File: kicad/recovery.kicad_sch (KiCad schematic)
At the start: 88 parts, among them CN1 S08B-PASK-2(LF)(SN), J1 Bus_PCI_Express_x1, J2 wago 2060-452/998-404, J3 wago 2060-452/998-404, J4 Conn_01x04, J5 Conn_01x02_Pin, J6 USB_C_Receptacle_USB2.0_16P, Q1 SI7232DN-T1-GE3, Q2 AO3400A, Q3 AO3400A, U1 MCP6002T-I/SN, U12 S03B-PASK-2, U13 S03B-PASK-2, U2 RP2040, U4 W25Q128JVP, U5 TPS22976DPUR, U6 GAQY252G3S, U9 MCP25625T-E/ML, X1 RP2040 Crystal, Y2 X322516MLB4SI

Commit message: feat: overhauled recovery board: added servos, solenoids, PWM-level shifters and firing circuit to layout
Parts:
- removed C2, C3: 100pF, PCM_JLCPCB:C_0402, symbol PCM_JLCPCB-Capacitors:0402,100pF
- removed C31: 22nF, PCM_JLCPCB:C_0603, symbol PCM_JLCPCB-Capacitors:0603,22nF
- removed CN1: S08B-PASK-2(LF)(SN), easyeda2kicad:CONN-TH_S08B-PASK-2, symbol easyeda2kicad:S08B-PASK-2(LF)(SN)
- removed R1, R9: 100Ω, PCM_JLCPCB:R_0402, symbol PCM_JLCPCB-Resistors:0402,100Ω
- removed R203, R204: 27, Resistor_SMD:R_0402_1005Metric, symbol Device:R
- removed R29, R34: 5.1Ω, PCM_JLCPCB:R_0603, symbol PCM_JLCPCB-Resistors:0603,5.1Ω
- removed U12: S03B-PASK-2, easyeda2kicad:CONN-TH_S03B-PASK-2-LF-SN, symbol easyeda2kicad:S03B-PASK-2(LF)(SN)
- added C2, C4: 100pF, PCM_JLCPCB:C_0603, symbol PCM_JLCPCB-Capacitors:0603,100pF
- added C3, C5, C6, C7, C8: 100u, Capacitor_SMD:C_1210_3225Metric, symbol Device:C
- added R1, R36: 100Ω, PCM_JLCPCB:R_0603, symbol PCM_JLCPCB-Resistors:0603,100Ω
- added R35: 27Ω, PCM_JLCPCB:R_0603, symbol PCM_JLCPCB-Resistors:0603,27Ω
- added U10: S03B-PASK-2, easyeda2kicad:CONN-TH_S03B-PASK-2-LF-SN, symbol easyeda2kicad:S03B-PASK-2(LF)(SN)
- added U3, U7: MOF5WS-5.1Ω±5% T, easyeda2kicad:RES-TH_BD6.0-L17.5-P21.50-D0.7, symbol easyeda2kicad:MOF5WS-5.1Ω±5%T
- added U8: S05B-PASK-2(LF)(SN), easyeda2kicad:CONN-TH_S05B-PASK-2-LF-SN, symbol easyeda2kicad:S05B-PASK-2(LF)(SN)
- R11: now fitted
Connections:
- net +5V_Servo is gone; now on net +5V: C21.1, C28.1, R19.2, R24.2, U5.1 (VIN1), U5.2 (VIN1), U5.4 (VBIAS), U5.6 (VIN2), U5.7 (VIN2)
- net AIN_0IN is gone; now on net PT_IN1: U13.2
- net AIN_1IN is gone; now on net PT_IN2: U13.3
- net +24V: now also U10.3
- net +3.3V: no longer R10.1, R15.1, R16.2, R17.2, R18.1
- net +5V: now also C3.1, C5.1, C6.1, C7.1, C8.1
- net 5V_PWM1: now also U8.5
- net 5V_PWM2: now also U8.1
- net CANSTBY: now also U2.18 (GPIO15)
- net GND: now also C2.2, C3.2, C4.2, C5.2, C6.2, C7.2, C8.2, U10.1, U10.2, U8.3; no longer R11.2
- net OUTA: now also R36.2
- net OUTB: now also R1.2
- net PT_1: now also C4.1, R36.1
- net PT_2: now also C2.1, R1.1
- net SERVO_PWR1: now also U8.4
- net SERVO_PWR2: now also U8.2
- net SWCLK: now also J4.2 (Pin_2); no longer J4.1 (Pin_1)
- net SWD: now also J4.1 (Pin_1); no longer J4.2 (Pin_2)
- net USB_D+: now also R35.1
- net USB_D-: now also R11.1
- net USB_D2+: now also R35.2
- net USB_D2-: now also R11.2
- net at Q1.7, Q1.8, R32.2: now also U7.1
- net at Q1.5, Q1.6, R22.2: now also U3.1
- net MCU_SOLENOID: now reaches U2.3 (GPIO1)
- net MCU_SOLENOID: now also R10.1
- net at J2.1 (1_1), J2.2 (1_2): now also U7.2
- net at J3.1 (1_1), J3.2 (1_2): now also U3.2
- new net MCU_PWM1: R15.1, R16.2
- new net MCU_PWM2: R17.2, R18.1
- no-connect marks 35 -> 31
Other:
- moved on the sheet: C1, J4, U13

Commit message: Feat: Completed layout, modified divider network for 5V PT operation
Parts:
- removed C21, C28: 1uF, PCM_JLCPCB:C_0603, symbol PCM_JLCPCB-Capacitors:0603,1uF
- removed C29, C30: 100nF, PCM_JLCPCB:C_0402, symbol PCM_JLCPCB-Capacitors:0402,100nF
- removed C5, C6, C7, C8: 100u, Capacitor_SMD:C_1210_3225Metric, symbol Device:C
- removed R13, R14, R16, R17, R19, R24: 5.1kΩ, PCM_JLCPCB:R_0603, symbol PCM_JLCPCB-Resistors:0603,5.1kΩ
- removed R15, R18: 120Ω, PCM_JLCPCB:R_0603, symbol PCM_JLCPCB-Resistors:0603,120Ω
- removed R25: 10kΩ, PCM_JLCPCB:R_0402, symbol PCM_JLCPCB-Resistors:0402,10kΩ
- removed R27, R28: 10Ω, PCM_JLCPCB:R_0603, symbol PCM_JLCPCB-Resistors:0603,10Ω
- removed R5, R7: 100kΩ, PCM_JLCPCB:R_0402, symbol PCM_JLCPCB-Resistors:0402,100kΩ
- removed R6, R8: 33kΩ, PCM_JLCPCB:R_0402, symbol PCM_JLCPCB-Resistors:0402,33kΩ
- removed U10: S03B-PASK-2, easyeda2kicad:CONN-TH_S03B-PASK-2-LF-SN, symbol easyeda2kicad:S03B-PASK-2(LF)(SN)
- removed U5: TPS22976DPUR, easyeda2kicad:WSON-14_L3.0-W2.0-P0.40-BL-EP-1, symbol easyeda2kicad:TPS22976DPUR
- removed U8: S05B-PASK-2(LF)(SN), easyeda2kicad:CONN-TH_S05B-PASK-2-LF-SN, symbol easyeda2kicad:S05B-PASK-2(LF)(SN)
- added C12, C13, C9: 100u, Capacitor_SMD:C_1210_3225Metric, symbol Device:C
- added C5, C6, C7, C8: 1uF, PCM_JLCPCB:C_0402, symbol PCM_JLCPCB-Capacitors:0402,1uF
- added CN1: S06B-PASK-2(LF)(SN), easyeda2kicad:CONN-TH_6P-P2.00_S06B-PASK-2-LF-SN, symbol easyeda2kicad:S06B-PASK-2(LF)(SN)
- added R13, R14, R9: 10kΩ, PCM_JLCPCB:R_0402, symbol PCM_JLCPCB-Resistors:0402,10kΩ
- added R15, R16: 1k, Resistor_SMD:R_0402_1005Metric, symbol Device:R
- added R18, R6: 100kΩ, PCM_JLCPCB:R_0603, symbol PCM_JLCPCB-Resistors:0603,100kΩ
- added R5, R7: 51kΩ, PCM_JLCPCB:R_0603, symbol PCM_JLCPCB-Resistors:0603,51kΩ
- added U11, U5: TMI6240, easyeda2kicad:SOT-23-5_L2.9-W1.6-P0.95-LS2.8-BL, symbol easyeda2kicad:TMI6240
- added U8: S02B-PASK-2(LF)(SN), easyeda2kicad:CONN-TH_S02B-PASK-2-LF-SN, symbol easyeda2kicad:S02B-PASK-2(LF)(SN)
- C1, C3: LCSC (none) -> C23742
- C10, C11: LCSC (none) -> C1548
- C2, C4: LCSC PN (none) -> C14858
- C206, C207, C209, C211, C212, C213, C214, C215, C216, C40, C90, C92, C93: LCSC (none) -> C307331
- C208, C210: LCSC (none) -> C52923
- C94, C95: LCSC (none) -> C1555
- D1: LCSC (none) -> C2286
- D2: LCSC PN (none) -> C14996
- J2, J3: LCSC (none) -> C2765055
- J6: LCSC (none) -> C2765186
- Q1: LCSC (none) -> C144854
- Q2, Q3: LCSC PN (none) -> C20917
- R1, R36: LCSC PN (none) -> C22775
- R10: LCSC PN (none) -> C23025
- R11, R35: LCSC PN (none) -> C25190
- R12, R2, R30: LCSC (none) -> C11702
- R20, R300: LCSC (none) -> C25076
- R21, R31: LCSC (none) -> C25890
- R22, R32: LCSC (none) -> C25741
- R23, R33: LCSC (none) -> C25551
- R3, R4: LCSC (none) -> C25905
- R91: LCSC (none) -> C25744
- S2: LCSC (none) -> C318884
- U1: LCSC (none) -> C7377
- U13: LCSC (none) -> C265095
- U2: LCSC (none) -> C2040
- U3, U7: LCSC (none) -> C121946
- U4: LCSC (none) -> C190862
- U6: LCSC (none) -> C7435106
- U9: LCSC (none) -> C191253
- X1: LCSC (none) -> C20625731
- Y2: LCSC (none) -> C12668
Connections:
- net 3.3V_PWM1 is gone; now on net MCU_PWM1: Q2.2 (S)
- net +24V: now also D2.1, U8.2; no longer D2.2
- net +3.3V: now also R9.2
- net +5V: now also R13.2, R14.2
- net 5V_PWM1: now also CN1.6, R13.1
- net 5V_PWM2: now also CN1.1, R14.1
- net GND: now also D2.2, U13.3, C12.2, C13.2, C5.1, C6.1, C7.1, C8.1, C9.2, CN1.3, CN1.4, R15.1, R16.1, R18.2, R6.2, U11.2 (GND), U5.2 (GND), U8.1; no longer D2.1, U13.1
- net MCU_PWM1: now also U2.37 (GPIO25), R15.2
- net MCU_PWM2: now also Q3.2 (S), U2.36 (GPIO24), R16.2
- net PT_IN1: now also U13.1, R7.1; no longer U13.2
- net PT_IN2: now also U13.2, R5.1; no longer U13.3
- net SERVO_ON1: now also U2.29 (GPIO18), U11.3 (EN)
- net SERVO_ON2: now also U2.32 (GPIO21), U5.3 (EN)
- net SERVO_PWR1: now also C8.2, CN1.5, U11.5 (VOUT)
- net SERVO_PWR2: now also C7.2, CN1.2, U5.5 (VOUT)
- net at Q2.1 (G): now also R9.1
- net at U1.5 (+INB): now also R5.2, R6.1
- net at Q3.1 (G): now also R26.1
- net at U1.3 (+INA): now also R18.1, R7.2
- removed net 3.3V_PWM2: Q3.2 (S), R26.1
- net CANH renamed CANP
- net CANL renamed CANN
- net v_lipo renamed v_servo
- net v_servo: now also C12.1, C13.1, C5.2, C6.2, C9.1, U11.1 (VIN), U5.1 (VIN)
- no-connect marks 31 -> 29
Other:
- note removed: "CAN"
- moved on the sheet: D2, R26, U13

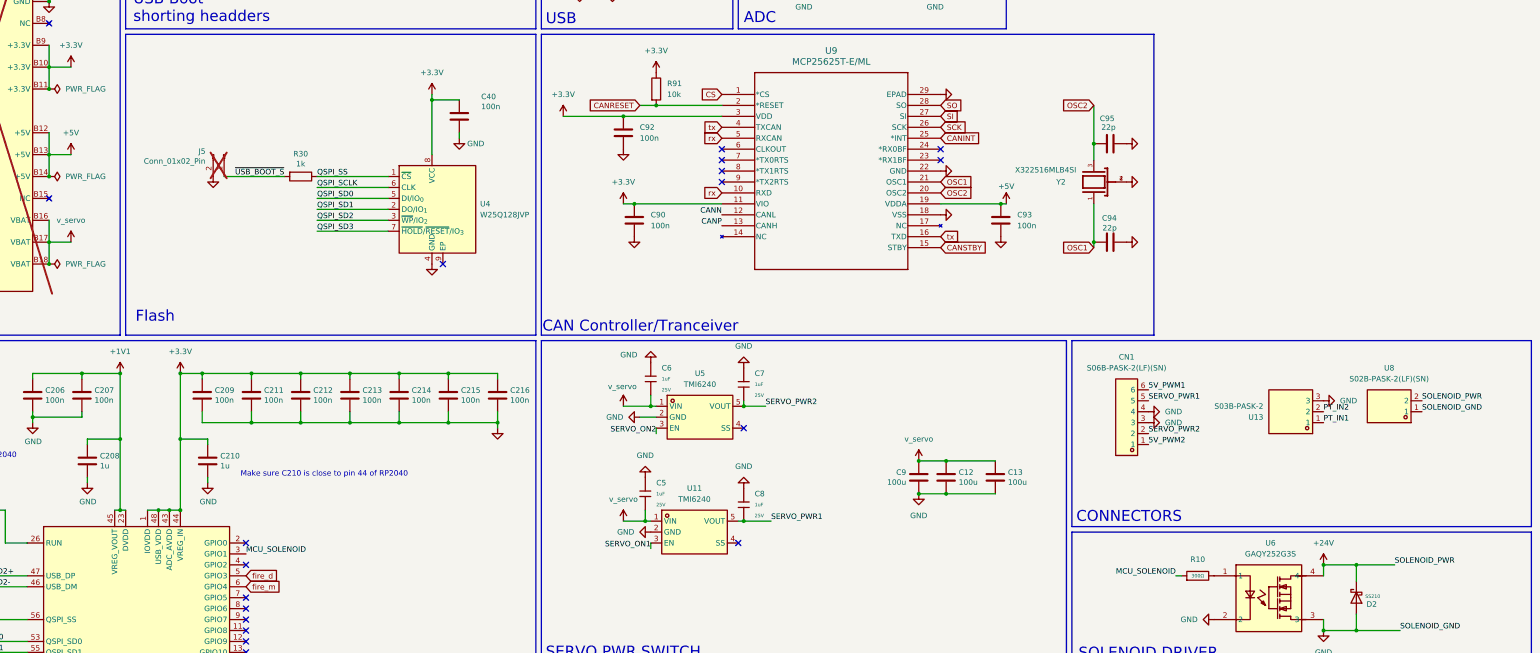
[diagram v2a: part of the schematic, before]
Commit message: fix: Reviewed components tolerances and BOM for version alpha
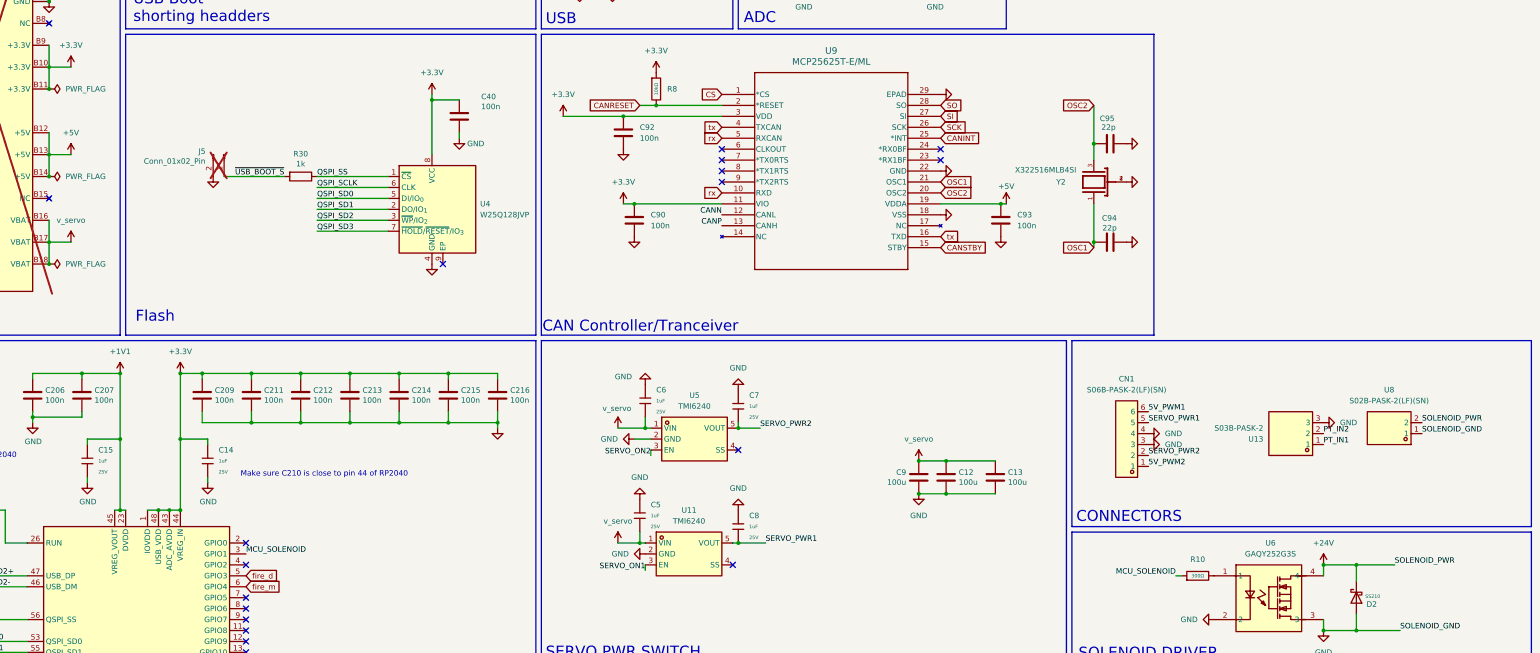
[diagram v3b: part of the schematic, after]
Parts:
- removed C208, C210: 1u, Capacitor_SMD:C_0402_1005Metric, symbol Device:C
- removed R91: 10k, Resistor_SMD:R_0402_1005Metric, symbol Device:R
- added C14, C15: 1uF, PCM_JLCPCB:C_0402, symbol PCM_JLCPCB-Capacitors:0402,1uF
- added R8: 10kΩ, PCM_JLCPCB:R_0402, symbol PCM_JLCPCB-Resistors:0402,10kΩ
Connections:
- net +1V1: now also C15.2
- net +3.3V: now also C14.1, R8.1
- net CANRESET: now also R8.2
- net GND: now also C14.2, C15.1
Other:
- moved on the sheet: C5, C6, C7, C8, CN1, U11, U13, U5, U8
